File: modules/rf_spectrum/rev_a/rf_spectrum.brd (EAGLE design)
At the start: 68.1 x 66 mm, 41 parts, among them J3 MODULE_GENERIC_DEBUGSMT, J4 TC2030-JLINK-L, U1 MWSUB3G, U2 SKY13317, U3 STM32L432KC, U4 TLV62130, X1 ABS05-32.768KHZ-T

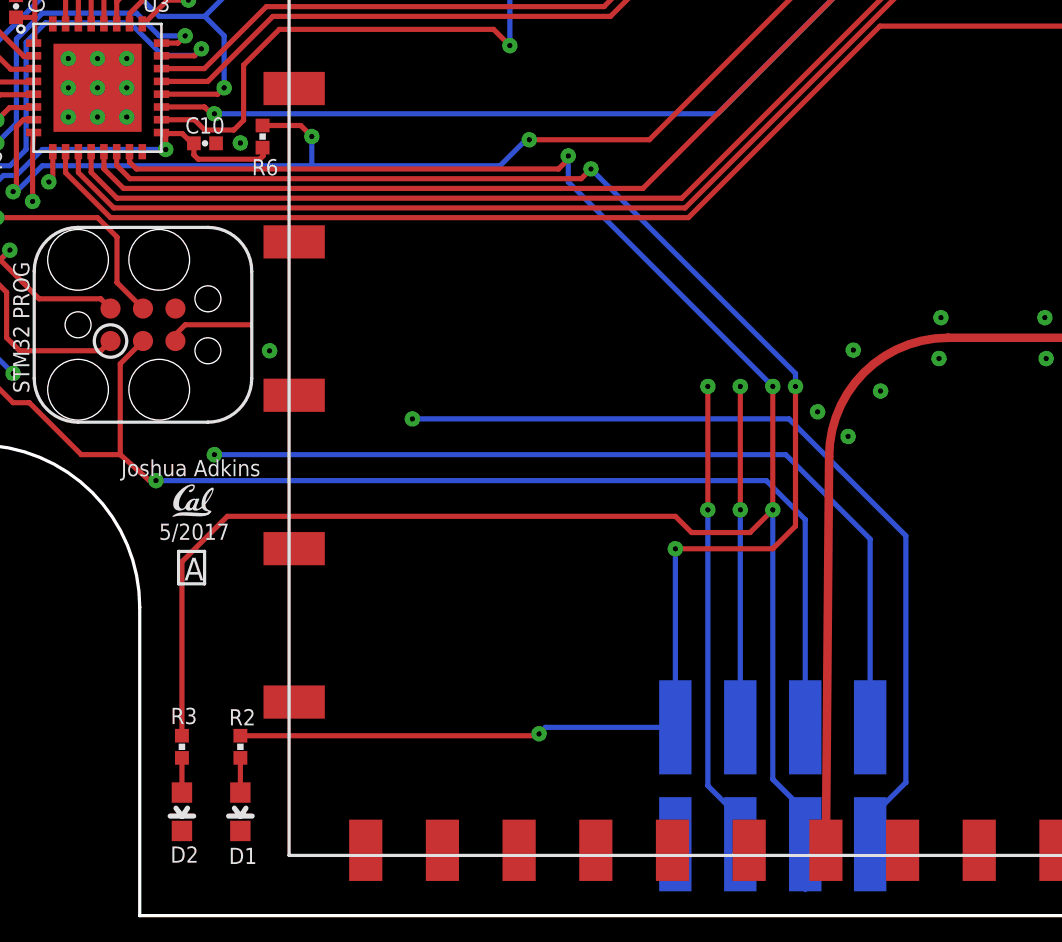
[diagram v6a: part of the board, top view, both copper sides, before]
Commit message: less traces under microstrip
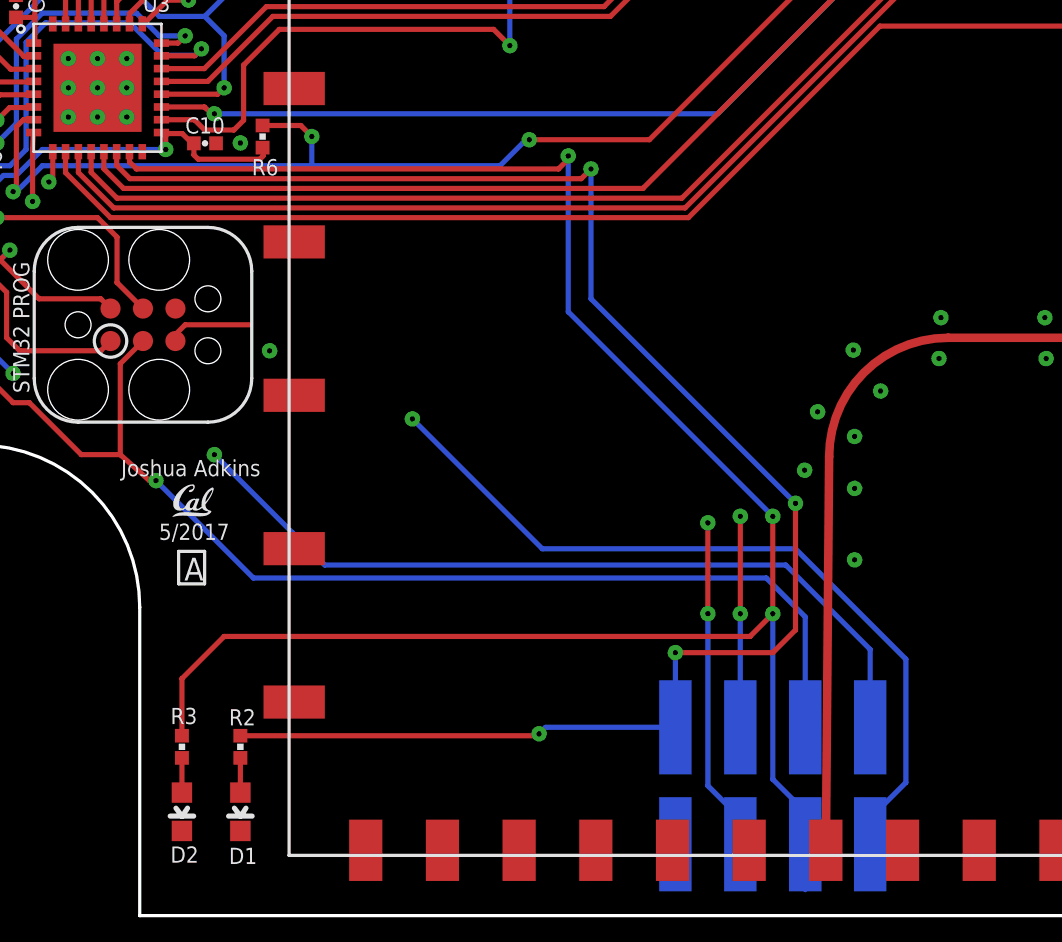
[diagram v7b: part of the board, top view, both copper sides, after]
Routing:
- net DBG_GPIO2: track 81.8 -> 76.9 mm
- net DBG_TX: track 50.6 -> 47.5 mm
- net DBG_RX: track 45.2 -> 42.2 mm
- net SWDCLK: track 77.3 -> 74.5 mm
- net SWDIO: track 74.7 -> 72.2 mm
- net !RST: track 63.7 -> 61.4 mm
- net GND: vias 78 -> 81
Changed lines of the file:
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@@
 <setting verticaltext="up"/>
 </settings>
-<grid distance="0.1" unitdist="mil" unit="mil" style="lines" multiple="1" display="yes" altdistance="0.01" altunitdist="mil" altunit="mil"/>
+<grid distance="0.01" unitdist="inch" unit="inch" style="lines" multiple="1" display="yes" altdistance="0.01" altunitdist="inch" altunit="inch"/>
 <layers>
 <layer number="1" name="Top" color="4" fill="1" visible="yes" active="yes"/>
@@
 <contactref element="ADBG" pad="2"/>
 <contactref element="ADBG" pad="5"/>
-<via x="39.5224" y="21.2852" extent="1-16" drill="0.2032"/>
+<via x="39.7764" y="21.2852" extent="1-16" drill="0.2032"/>
 <via x="38.3286" y="22.2504" extent="1-16" drill="0.2032"/>
 <via x="39.7256" y="24.6634" extent="1-16" drill="0.2032"/>
@@
 <via x="61.8236" y="42.9514" extent="1-16" drill="0.2032"/>
 <via x="5.207" y="32.004" extent="1-16" drill="0.2032"/>
+<via x="37.8206" y="19.9644" extent="1-16" drill="0.2032"/>
+<via x="39.7764" y="19.2532" extent="1-16" drill="0.2032"/>
+<via x="39.7764" y="16.4592" extent="1-16" drill="0.2032"/>
 </signal>
 <signal name="3V3">
@@
 <wire x1="6.196140625" y1="35.152140625" x2="7.637140625" y2="35.152140625" width="0.2032" layer="1"/>
 <wire x1="7.637140625" y1="35.152140625" x2="7.66" y2="35.175" width="0.2032" layer="1"/>
-<wire x1="37.846" y1="9.906" x2="37.846" y2="18.034" width="0.2032" layer="16"/>
-<wire x1="37.846" y1="18.034" x2="36.322" y2="19.558" width="0.2032" layer="16"/>
-<wire x1="36.322" y1="19.558" x2="12.446" y2="19.558" width="0.2032" layer="16"/>
+<wire x1="37.846" y1="9.906" x2="37.846" y2="14.224" width="0.2032" layer="16"/>
+<wire x1="37.846" y1="14.224" x2="36.322" y2="15.748" width="0.2032" layer="16"/>
+<wire x1="36.322" y1="15.748" x2="16.256" y2="15.748" width="0.2032" layer="16"/>
+<wire x1="16.256" y1="15.748" x2="12.446" y2="19.558" width="0.2032" layer="16"/>
 <via x="12.446" y="19.558" extent="1-16" drill="0.2032"/>
 <wire x1="12.446" y1="19.558" x2="12.192" y2="19.558" width="0.2032" layer="1"/>
@@
 <wire x1="6.35" y1="28.194" x2="5.207" y2="29.337" width="0.2032" layer="1"/>
 <wire x1="6.35" y1="28.194" x2="7.874" y2="26.67" width="0.2032" layer="1"/>
-<wire x1="40.386" y1="9.906" x2="40.386" y2="17.272" width="0.2032" layer="16"/>
-<wire x1="40.386" y1="17.272" x2="37.084" y2="20.574" width="0.2032" layer="16"/>
+<wire x1="40.386" y1="9.906" x2="40.386" y2="12.954" width="0.2032" layer="16"/>
+<wire x1="40.386" y1="12.954" x2="37.084" y2="16.256" width="0.2032" layer="16"/>
 <wire x1="6.096" y1="27.94" x2="6.096" y2="24.511" width="0.2032" layer="16"/>
 <via x="6.731" y="28.575" extent="1-16" drill="0.2032"/>
@@
 <wire x1="6.858" y1="23.241" x2="6.858" y2="23.749" width="0.2032" layer="15"/>
 <via x="6.858" y="23.749" extent="1-16" drill="0.2032"/>
-<wire x1="37.084" y1="20.574" x2="14.732" y2="20.574" width="0.2032" layer="16"/>
+<wire x1="37.084" y1="16.256" x2="19.05" y2="16.256" width="0.2032" layer="16"/>
+<wire x1="19.05" y1="16.256" x2="17.78" y2="17.526" width="0.2032" layer="16"/>
+<wire x1="17.78" y1="17.526" x2="14.732" y2="20.574" width="0.2032" layer="16"/>
 <wire x1="6.096" y1="24.511" x2="6.858" y2="23.749" width="0.2032" layer="16"/>
 </signal>
@@
 <wire x1="40.386" y1="5.334" x2="40.386" y2="6.35" width="0.2032" layer="16"/>
 <wire x1="40.386" y1="6.35" x2="41.783" y2="7.747" width="0.2032" layer="16"/>
-<wire x1="41.783" y1="7.747" x2="41.783" y2="17.399" width="0.2032" layer="16"/>
-<wire x1="41.783" y1="17.399" x2="37.211" y2="21.971" width="0.2032" layer="16"/>
-<wire x1="37.211" y1="21.971" x2="22.479" y2="21.971" width="0.2032" layer="16"/>
+<wire x1="41.783" y1="7.747" x2="41.783" y2="12.573" width="0.2032" layer="16"/>
+<wire x1="41.783" y1="12.573" x2="37.465" y2="16.891" width="0.2032" layer="16"/>
+<wire x1="37.465" y1="16.891" x2="27.559" y2="16.891" width="0.2032" layer="16"/>
+<wire x1="27.559" y1="16.891" x2="22.479" y2="21.971" width="0.2032" layer="16"/>
 <wire x1="22.479" y1="21.971" x2="14.605" y2="29.845" width="0.2032" layer="15"/>
 <wire x1="14.605" y1="29.845" x2="6.223" y2="29.845" width="0.2032" layer="15"/>
@@
 <wire x1="7.62" y1="30.48" x2="7.747" y2="30.48" width="0.2032" layer="15"/>
 <wire x1="7.747" y1="30.48" x2="8.001" y2="30.226" width="0.2032" layer="15"/>
-<wire x1="8.001" y1="30.226" x2="27.051" y2="30.226" width="0.2032" layer="15"/>
-<wire x1="27.051" y1="30.226" x2="34.036" y2="23.241" width="0.2032" layer="15"/>
+<wire x1="8.001" y1="30.226" x2="21.717" y2="30.226" width="0.2032" layer="15"/>
+<wire x1="21.717" y1="30.226" x2="34.036" y2="17.907" width="0.2032" layer="15"/>
 <wire x1="35.306" y1="5.334" x2="35.306" y2="6.35" width="0.2032" layer="16"/>
 <wire x1="35.306" y1="6.35" x2="34.036" y2="7.62" width="0.2032" layer="16"/>
-<wire x1="34.036" y1="7.62" x2="34.036" y2="18.415" width="0.2032" layer="16"/>
-<via x="34.036" y="18.415" extent="1-16" drill="0.2032"/>
-<wire x1="34.036" y1="18.415" x2="34.036" y2="23.241" width="0.2032" layer="1"/>
-<via x="34.036" y="23.241" extent="1-16" drill="0.2032"/>
+<wire x1="34.036" y1="7.62" x2="34.036" y2="14.351" width="0.2032" layer="16"/>
+<via x="34.036" y="14.351" extent="1-16" drill="0.2032"/>
+<wire x1="34.036" y1="14.351" x2="34.036" y2="17.907" width="0.2032" layer="1"/>
+<via x="34.036" y="17.907" extent="1-16" drill="0.2032"/>
 </signal>
 <signal name="DBG_RX">
@@
 <wire x1="8.255" y1="31.242" x2="8.255" y2="30.861" width="0.2032" layer="15"/>
 <wire x1="8.255" y1="30.861" x2="8.509" y2="30.607" width="0.2032" layer="15"/>
-<wire x1="8.509" y1="30.607" x2="27.94" y2="30.607" width="0.2032" layer="15"/>
-<wire x1="27.94" y1="30.607" x2="35.306" y2="23.241" width="0.2032" layer="15"/>
-<via x="35.306" y="18.415" extent="1-16" drill="0.2032"/>
-<via x="35.306" y="23.241" extent="1-16" drill="0.2032"/>
-<wire x1="35.306" y1="9.906" x2="35.306" y2="18.415" width="0.2032" layer="16"/>
-<wire x1="35.306" y1="18.415" x2="35.306" y2="23.241" width="0.2032" layer="1"/>
+<wire x1="8.509" y1="30.607" x2="22.86" y2="30.607" width="0.2032" layer="15"/>
+<wire x1="22.86" y1="30.607" x2="35.306" y2="18.161" width="0.2032" layer="15"/>
+<via x="35.306" y="14.351" extent="1-16" drill="0.2032"/>
+<via x="35.306" y="18.161" extent="1-16" drill="0.2032"/>
+<wire x1="35.306" y1="9.906" x2="35.306" y2="14.351" width="0.2032" layer="16"/>
+<wire x1="35.306" y1="14.351" x2="35.306" y2="18.161" width="0.2032" layer="1"/>
 </signal>
 <signal name="DBG_GPIO1">
@@
 <via x="29.464" y="31.75" extent="1-16" drill="0.2032"/>
 <wire x1="11.43" y1="31.369" x2="29.083" y2="31.369" width="0.2032" layer="1"/>
-<via x="32.766" y="16.891" extent="1-16" drill="0.2032"/>
-<wire x1="32.766" y1="9.906" x2="32.766" y2="16.891" width="0.2032" layer="16"/>
-<wire x1="32.766" y1="16.891" x2="36.576" y2="16.891" width="0.2032" layer="1"/>
-<wire x1="36.576" y1="16.891" x2="37.465" y2="17.78" width="0.2032" layer="1"/>
-<via x="37.465" y="23.241" extent="1-16" drill="0.2032"/>
-<wire x1="37.465" y1="23.241" x2="37.465" y2="23.749" width="0.2032" layer="16"/>
-<wire x1="37.465" y1="23.749" x2="29.464" y2="31.75" width="0.2032" layer="16"/>
-<wire x1="37.465" y1="17.78" x2="37.465" y2="23.241" width="0.2032" layer="1"/>
+<via x="32.766" y="12.827" extent="1-16" drill="0.2032"/>
+<wire x1="32.766" y1="9.906" x2="32.766" y2="12.827" width="0.2032" layer="16"/>
+<wire x1="32.766" y1="12.827" x2="36.576" y2="12.827" width="0.2032" layer="1"/>
+<wire x1="36.576" y1="12.827" x2="37.465" y2="13.716" width="0.2032" layer="1"/>
+<via x="37.465" y="18.669" extent="1-16" drill="0.2032"/>
+<wire x1="37.465" y1="18.669" x2="29.464" y2="26.67" width="0.2032" layer="16"/>
+<wire x1="29.464" y1="26.67" x2="29.464" y2="31.75" width="0.2032" layer="16"/>
+<wire x1="37.465" y1="13.716" x2="37.465" y2="18.669" width="0.2032" layer="1"/>
 </signal>
 <signal name="DBG_GPIO2">
@@
 <wire x1="37.846" y1="5.334" x2="37.846" y2="6.604" width="0.2032" layer="16"/>
 <wire x1="37.846" y1="6.604" x2="36.576" y2="7.874" width="0.2032" layer="16"/>
-<wire x1="36.576" y1="18.415" x2="36.576" y2="7.874" width="0.2032" layer="16"/>
+<wire x1="36.576" y1="14.351" x2="36.576" y2="7.874" width="0.2032" layer="16"/>
 <wire x1="28.194" y1="31.75" x2="28.575" y2="32.131" width="0.2032" layer="1"/>
 <wire x1="28.575" y1="32.131" x2="28.575" y2="32.258" width="0.2032" layer="1"/>
 <via x="28.575" y="32.258" extent="1-16" drill="0.2032"/>
-<wire x1="28.575" y1="32.258" x2="28.575" y2="31.242" width="0.2032" layer="16"/>
-<wire x1="28.575" y1="31.242" x2="36.576" y2="23.241" width="0.2032" layer="16"/>
-<via x="36.576" y="23.241" extent="1-16" drill="0.2032"/>
-<wire x1="36.576" y1="18.415" x2="36.576" y2="23.241" width="0.2032" layer="1"/>
-<via x="36.576" y="18.415" extent="1-16" drill="0.2032"/>
-<wire x1="13.462" y1="16.383" x2="15.24" y2="18.161" width="0.2032" layer="1"/>
-<wire x1="15.24" y1="18.161" x2="32.766" y2="18.161" width="0.2032" layer="1"/>
-<wire x1="32.766" y1="18.161" x2="33.401" y2="17.526" width="0.2032" layer="1"/>
-<wire x1="33.401" y1="17.526" x2="35.687" y2="17.526" width="0.2032" layer="1"/>
-<wire x1="35.687" y1="17.526" x2="36.576" y2="18.415" width="0.2032" layer="1"/>
-<wire x1="13.462" y1="9.57706875" x2="13.462" y2="16.383" width="0.2032" layer="1"/>
+<wire x1="28.575" y1="32.258" x2="28.575" y2="26.162" width="0.2032" layer="16"/>
+<wire x1="28.575" y1="26.162" x2="36.576" y2="18.161" width="0.2032" layer="16"/>
+<via x="36.576" y="18.161" extent="1-16" drill="0.2032"/>
+<wire x1="36.576" y1="14.351" x2="36.576" y2="18.161" width="0.2032" layer="1"/>
+<via x="36.576" y="14.351" extent="1-16" drill="0.2032"/>
+<wire x1="36.576" y1="14.351" x2="35.687" y2="13.462" width="0.2032" layer="1"/>
+<wire x1="13.462" y1="11.811" x2="13.462" y2="9.57706875" width="0.2032" layer="1"/>
+<wire x1="15.113" y1="13.462" x2="13.462" y2="11.811" width="0.2032" layer="1"/>
+<wire x1="35.687" y1="13.462" x2="15.113" y2="13.462" width="0.2032" layer="1"/>
 </signal>
 <signal name="N$12">

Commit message: moved resistor
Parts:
- added R9: 750k, passives:0603-RES
- R7: value 240k -> 100k; device passives:0603-RES -> passives:0402_RES
- R8: value 750k -> 240k
- moved R7 9.86 mm to (14.5, 43.2), turned to 180 degrees
- moved R8 1.52 mm to (4.83, 45.2), turned to 0 degrees
- moved R6 0.44 mm to (16.3, 32.8), turned to 180 degrees
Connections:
- net !RF_RESET: now also U1.44, U3.18; no longer U1.P$44, U3.P$18
- net !RST: now also U3.4; no longer U3.P$4
- net 3V3: now also R7.2, R9.2, U1.31, U1.32, U1.33, U3.1, U3.17, U3.5; no longer R8.2, U1.P$31, U1.P$32, U1.P$33, U3.P$1, U3.P$17, U3.P$5
- net DBG_GPIO1: now also U3.14; no longer U3.P$14
- net DBG_GPIO2: now also U3.15; no longer U3.P$15
- net DBG_RX: now also U3.9; no longer U3.P$9
- net DBG_TX: now also U3.8; no longer U3.P$8
- net GND: now also R8.1, U1.10, U1.11, U1.12, U1.13, U1.14, U1.15, U1.16, U1.18, U1.20, U1.21, U1.22, U1.24, U1.26, U1.27, U1.28, U1.29, U1.34, U1.43, U1.45, U1.46, U1.5, U1.6, U1.7, U1.8, U1.9, U2.PAD, U3.16, U3.32, U3.THERMAL; no longer R7.1, U1.P$10, U1.P$11, U1.P$12, U1.P$13, U1.P$14, U1.P$15, U1.P$16, U1.P$18, U1.P$20, U1.P$21, U1.P$22, U1.P$24, U1.P$26, U1.P$27, U1.P$28, U1.P$29, U1.P$34, U1.P$43, U1.P$45, U1.P$46, U1.P$5, U1.P$6, U1.P$7, U1.P$8, U1.P$9, U2.P$1, U3.P$16, U3.P$32, U3.P$33
- net MOD_IN: now also U3.28; no longer U3.P$28
- net MOD_OUT: now also U3.26; no longer U3.P$26
- net N$1: now also U1.17; no longer U1.P$17
- net N$10: now also U3.3; no longer U3.P$3
- net N$11: now also U3.31; no longer U3.P$31
- net N$37: now also R8.2, R9.1; no longer R7.2, R8.1
- net N$9: now also U3.2; no longer U3.P$2
- net PPS: now also U3.6; no longer U3.P$6
- net RF_ANT1: now also U3.10; no longer U3.P$10
- net RF_ANT2: now also U3.11; no longer U3.P$11
- net RF_ANT3: now also U3.12; no longer U3.P$12
- net RF_GPIO2: now also R7.1, U1.3, U3.25; no longer U1.P$3, U3.P$25
- net RF_GPIO3: now also U1.37, U3.7; no longer U1.P$37, U3.P$7
- net RF_RX: now also U1.38, U3.29; no longer U1.P$38, U3.P$29
- net RF_TX: now also U1.39, U3.30; no longer U1.P$39, U3.P$30
- net SCL: now also U3.13, U3.19; no longer U3.P$13, U3.P$19
- net SDA: now also U3.20, U3.27; no longer U3.P$20, U3.P$27
- net SWDCLK: now also U3.24; no longer U3.P$24
- net SWDIO: now also U3.23; no longer U3.P$23
- net USB+: now also U3.22; no longer U3.P$22
- net USB-: now also U3.21; no longer U3.P$21
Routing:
- net RF_GPIO2: track 28.1 -> 31.4 mm
- net !RF_RESET: track 45.3 -> 44.7 mm
- net SWDIO: track 72.2 -> 71.7 mm
- net RF_GPIO3: track 71.8 -> 71.3 mm
